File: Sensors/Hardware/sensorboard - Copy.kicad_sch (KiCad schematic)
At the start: 75 parts, among them J15 Conn_Coaxial, U3 TPS61092RSAR

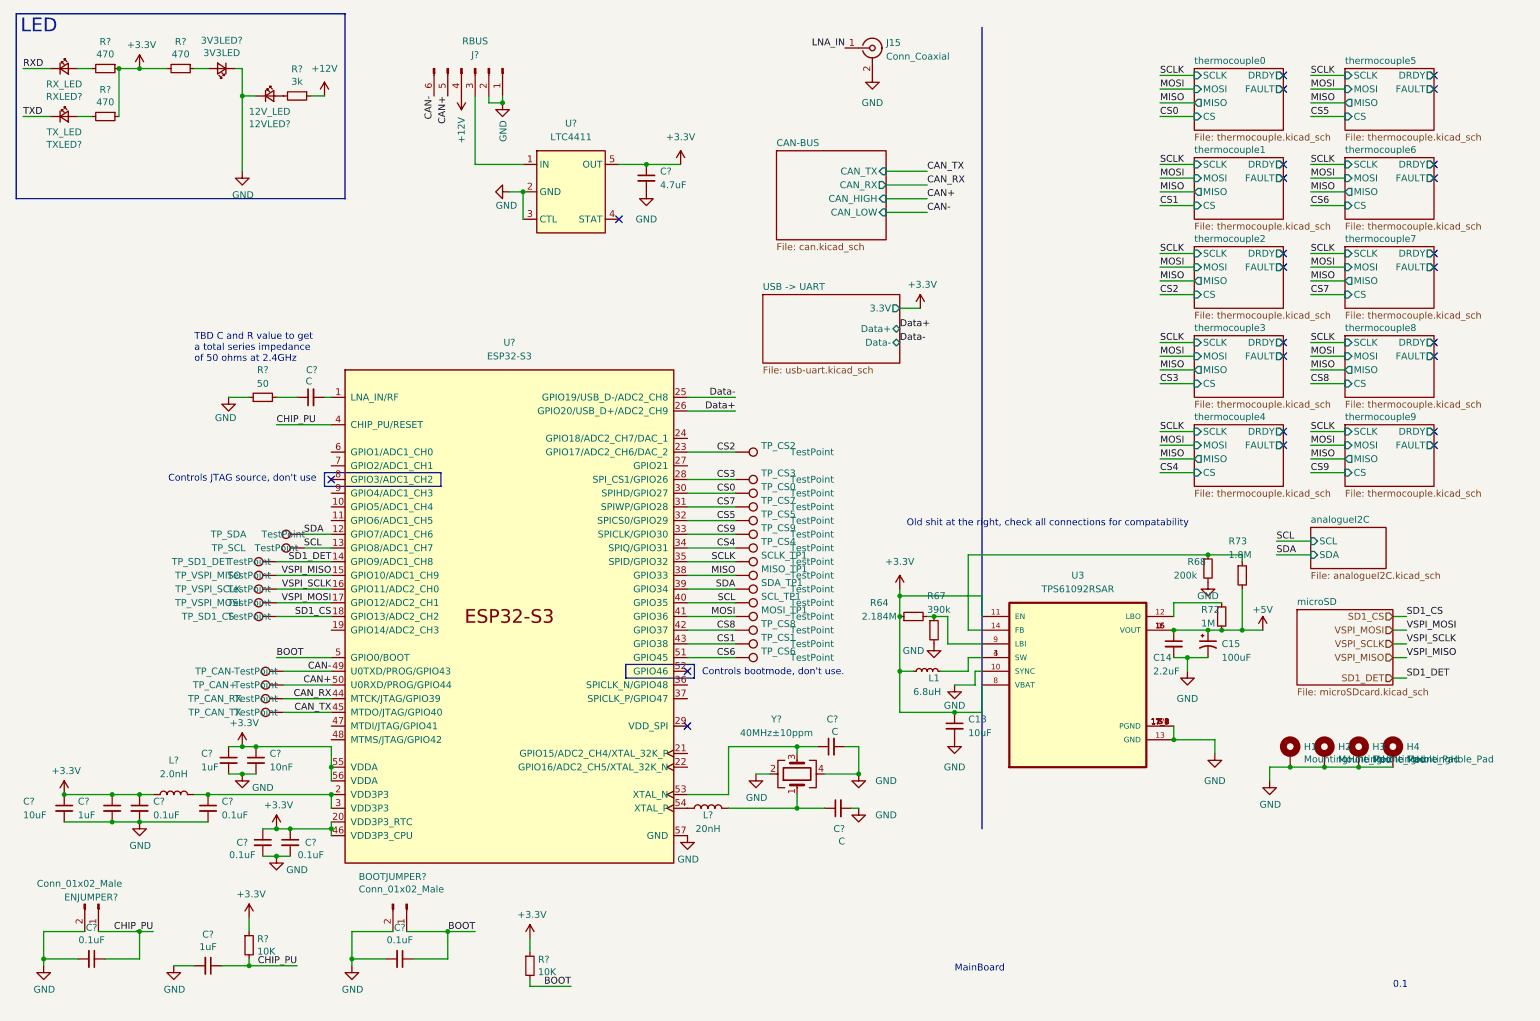
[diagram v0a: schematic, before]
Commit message: integrated new ESP32-s3
Need to remove excess thermocouples
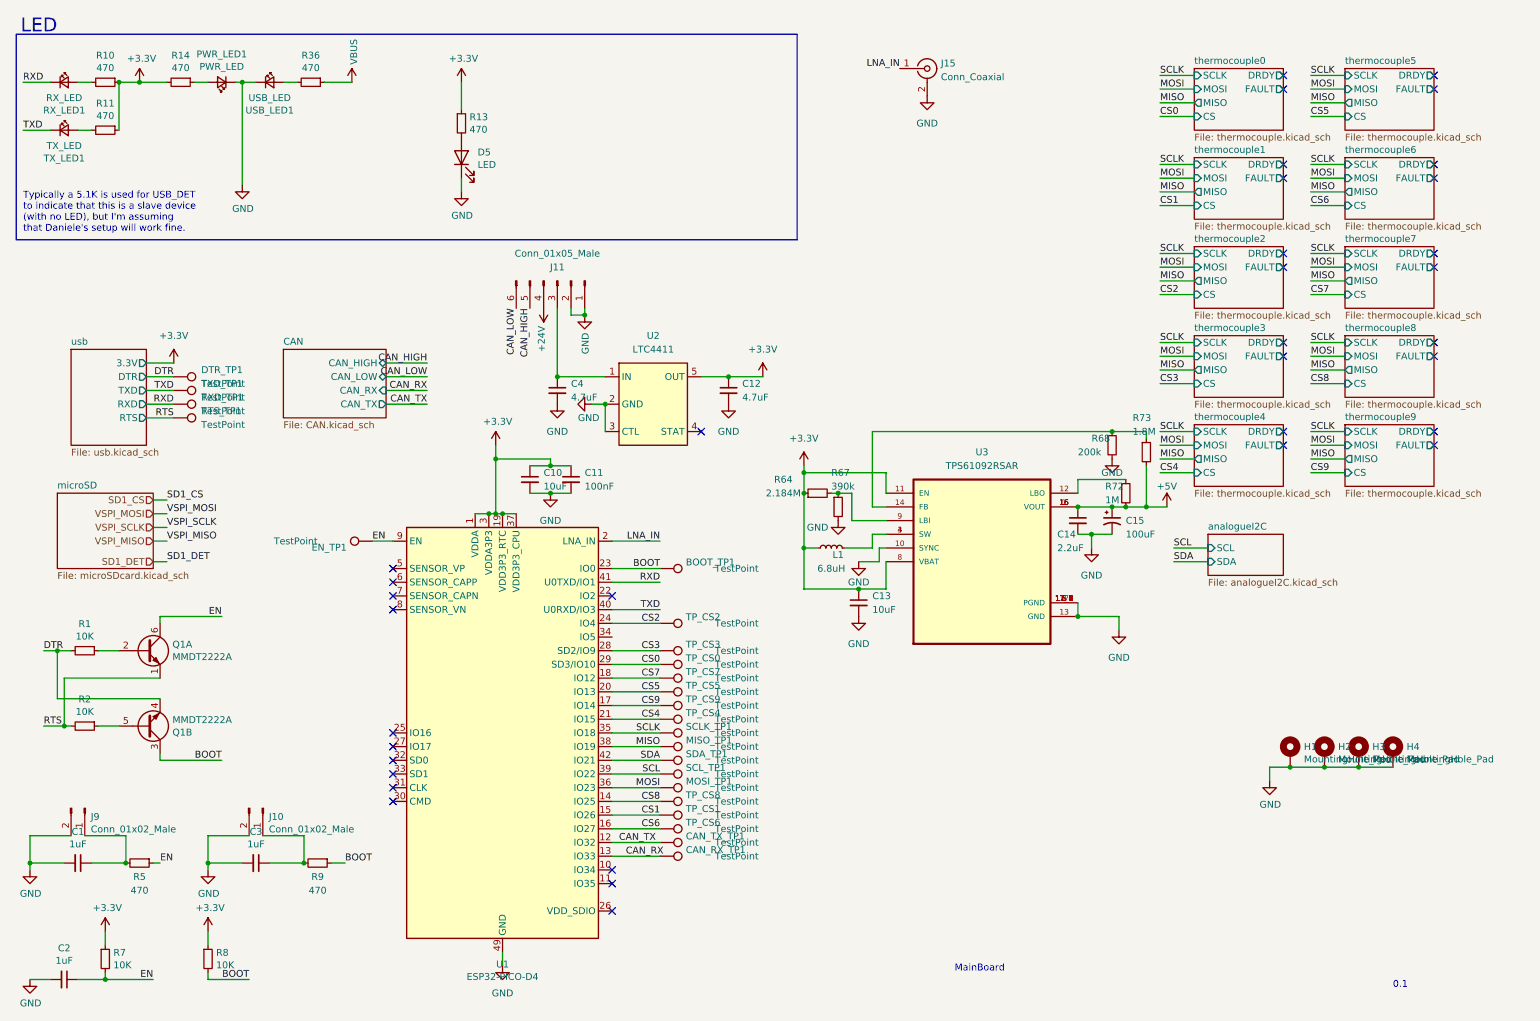
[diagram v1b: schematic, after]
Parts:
- removed 12VLED?: 12V_LED, Resistor_SMD:R_0402_1005Metric, symbol Device:LED_Small
- removed 3V3LED?: 3V3LED, Resistor_SMD:R_0402_1005Metric, symbol Device:LED_Small
- removed BOOTJUMPER?, ENJUMPER?: Conn_01x02_Male, Connector_PinHeader_2.54mm:PinHeader_1x02_P2.54mm_Vertical, symbol Connector:Conn_01x02_Male
- removed C? (x6): 0.1uF, Capacitor_SMD:C_0402_1005Metric, symbol Device:C_Small
- removed C? (x3): C, Capacitor_SMD:C_0603_1608Metric, symbol Device:C_Small
- removed C? (x3): 1uF, Capacitor_SMD:C_0402_1005Metric, symbol Device:C_Small
- removed C?: 10nF, Capacitor_SMD:C_0402_1005Metric, symbol Device:C_Small
- removed C?: 10uF, symbol Device:C_Small
- removed C?: 4.7uF, Capacitor_SMD:C_0603_1608Metric, symbol Device:C_Small
- removed J?: RBUS, Connector_Molex:Molex_Mini-Fit_Jr_5566-06A_2x03_P4.20mm_Vertical, symbol Connector:Conn_01x06_Male
- removed L?: 20nH, symbol Device:L
- removed L?: 2.0nH, symbol Device:L
- removed R? (x2): 10K, Resistor_SMD:R_0402_1005Metric, symbol Device:R_Small
- removed R?: 3k, Resistor_SMD:R_0402_1005Metric, symbol Device:R_Small
- removed R? (x3): 470, Resistor_SMD:R_0402_1005Metric, symbol Device:R_Small
- removed R?: 50, symbol Device:R_Small
- removed RXLED?: RX_LED, LED_SMD:LED_0603_1608Metric, symbol Device:LED_Small
- removed TP_CAN+, TP_CAN-, TP_CAN_RX, TP_CAN_TX, TP_SCL, TP_SD1_CS, TP_SD1_DET, TP_SDA, TP_VSPI_MISO, TP_VSPI_MOSI, TP_VSPI_SCLK: TestPoint, symbol Connector:TestPoint
- removed TXLED?: TX_LED, Resistor_SMD:R_0402_1005Metric, symbol Device:LED_Small
- removed U?: LTC4411, Package_TO_SOT_SMD:SOT-23-5, symbol iclr:LTC4411
- removed U?: ESP32-S3, Package_DFN_QFN:QFN-56-1EP_7x7mm_P0.4mm_EP5.6x5.6mm, symbol Espressif:ESP32-S3
- removed Y?: 40MHz±10ppm, Crystal:Crystal_SMD_2016-4Pin_2.0x1.6mm, symbol Device:Crystal_GND24
- added BOOT_TP1, CAN_RX_TP1, CAN_TX_TP1, DTR_TP1, EN_TP1, RTS_TP1, RXD_TP1, TXD_TP1: TestPoint, TestPoint:TestPoint_Pad_D1.0mm, symbol Connector:TestPoint
- added C1, C2, C3: 1uF, Capacitor_SMD:C_0603_1608Metric, symbol Device:C_Small
- added C10: 10uF, Capacitor_SMD:C_0603_1608Metric, symbol Device:C_Small
- added C11: 100nF, Capacitor_SMD:C_0603_1608Metric, symbol Device:C_Small
- added C12, C4: 4.7uF, Capacitor_SMD:C_0603_1608Metric, symbol Device:C_Small
- added D5: LED, LED_SMD:LED_0603_1608Metric, symbol Device:LED
- added J10, J9: Conn_01x02_Male, Connector_PinHeader_2.54mm:PinHeader_1x02_P2.54mm_Vertical, symbol Connector:Conn_01x02_Male
- added J11: Conn_01x05_Male, Connector_Molex:Molex_Mini-Fit_Jr_5566-06A_2x03_P4.20mm_Vertical, symbol Connector:Conn_01x06_Male
- added PWR_LED1: PWR_LED, LED_SMD:LED_0603_1608Metric, symbol Device:LED_Small
- added Q1: MMDT2222A, Package_TO_SOT_SMD:SOT-363_SC-70-6, symbol Transistor_BJT:MMDT2222A
- added R1, R2, R7, R8: 10K, Resistor_SMD:R_0603_1608Metric, symbol Device:R_Small
- added R10, R11, R13, R14, R36, R5, R9: 470, Resistor_SMD:R_0603_1608Metric, symbol Device:R_Small
- added RX_LED1: RX_LED, LED_SMD:LED_0603_1608Metric, symbol Device:LED_Small
- added TX_LED1: TX_LED, LED_SMD:LED_0603_1608Metric, symbol Device:LED_Small
- added U1: ESP32-PICO-D4, Package_DFN_QFN:QFN-48-1EP_7x7mm_P0.5mm_EP5.3x5.3mm, symbol RF_Module:ESP32-PICO-D4
- added U2: LTC4411, Package_TO_SOT_SMD:SOT-23-5, symbol iclr:LTC4411
- added USB_LED1: USB_LED, LED_SMD:LED_0603_1608Metric, symbol Device:LED_Small
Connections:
- net +3V3: now also C10.1, C11.1, C12.1, R10.1, R11.1, R13.1, R14.2, R7.1, R8.1, U1.1 (VDDA), U1.19 (VDD3P3_RTC), U1.3 (VDDA3P3), U1.37 (VDD3P3_CPU), U1.4 (VDDA3P3), U1.43 (VDDA), U1.46 (VDDA), U2.5 (OUT)
- net BOOT: now also BOOT_TP1.1, Q1.3 (C2), R8.2, R9.1, U1.23 (IO0)
- net CAN_RX: now also CAN_RX_TP1.1, U1.13 (IO33)
- net CAN_TX: now also CAN_TX_TP1.1, U1.12 (IO32)
- net CS0: now also U1.29 (SD3/IO10)
- net CS1: now also U1.15 (IO26)
- net CS2: now also U1.24 (IO4)
- net CS3: now also U1.28 (SD2/IO9)
- net CS4: now also U1.21 (IO15)
- net CS5: now also U1.20 (IO13)
- net CS6: now also U1.16 (IO27)
- net CS7: now also U1.18 (IO12)
- net CS8: now also U1.14 (IO25)
- net CS9: now also U1.17 (IO14)
- net GND: now also C1.2, C10.2, C11.2, C12.2, C2.2, C3.2, C4.2, D5.1 (K), J10.2 (Pin_2), J11.1 (Pin_1), J11.2 (Pin_2), J9.2 (Pin_2), PWR_LED1.1 (K), U1.49 (GND), U2.2 (GND), U2.3 (CTL), USB_LED1.1 (K)
- net LNA_IN: now also U1.2 (LNA_IN)
- net MISO: now also U1.38 (IO19)
- net MOSI: now also U1.36 (IO23)
- net RXD: now also RXD_TP1.1, RX_LED1.1 (K), U1.41 (U0TXD/IO1)
- net SCL: now also U1.39 (IO22)
- net SCLK: now also U1.35 (IO18)
- net SDA: now also U1.42 (IO21)
- net TXD: now also TXD_TP1.1, TX_LED1.1 (K), U1.40 (U0RXD/IO3)
- new net: C3.1, J10.1 (Pin_1), R9.2
- new net: C1.1, J9.1 (Pin_1), R5.2
- new net: R11.2, TX_LED1.2 (A)
- new net: R10.2, RX_LED1.2 (A)
- new net: Q1.2 (B1), R1.1
- new net: Q1.5 (B2), R2.1
- new net: PWR_LED1.2 (A), R14.1
- new net: R36.2, USB_LED1.2 (A)
- new net: D5.2 (A), R13.2
- new net: C4.1, J11.3 (Pin_3), U2.1 (IN)
- new net +24V: J11.4 (Pin_4)
- new net CAN_HIGH: J11.5 (Pin_5)
- new net CAN_LOW: J11.6 (Pin_6)
- new net DTR: DTR_TP1.1, Q1.4 (E2), R1.2
- new net EN: C2.1, EN_TP1.1, Q1.6 (C1), R5.1, R7.2, U1.9 (EN)
- new net RTS: Q1.1 (E1), R2.2, RTS_TP1.1
- new net VBUS: R36.1
- no-connect marks 24 -> 35
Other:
- removed sheet CAN-BUS
- removed sheet USB -> UART
- added sheet CAN (CAN.kicad_sch)
- added sheet usb (usb.kicad_sch)
- note added: "Typically a 5.1K is used for USB_DET to indicate that this is a slave device (with no LED), but I'm assuming that Daniele's setup will work fine."
- note removed: "Controls JTAG source, don't use"
- note removed: "Controls bootmode, don't use."
- note removed: "Old shit at the right, check all connections for compatability"
- note removed: "TBD C and R value to get a total series impedance of 50 ohms at 2.4GHz"
- moved on the sheet: C13, C14, C15, J15, L1, MISO_TP1, MOSI_TP1, R64, R67, R68, R72, R73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
